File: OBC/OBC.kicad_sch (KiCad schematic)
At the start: 9 parts, among them J2 IDC1 (PMS-Raspi), J3 IDC2 (Raspi-TRU), J5 Conn_01x04, J6 Modo de operación, U1 MPU9250, U2 BMP280, U3 RASPBERRY_PI_ZERO_2_W

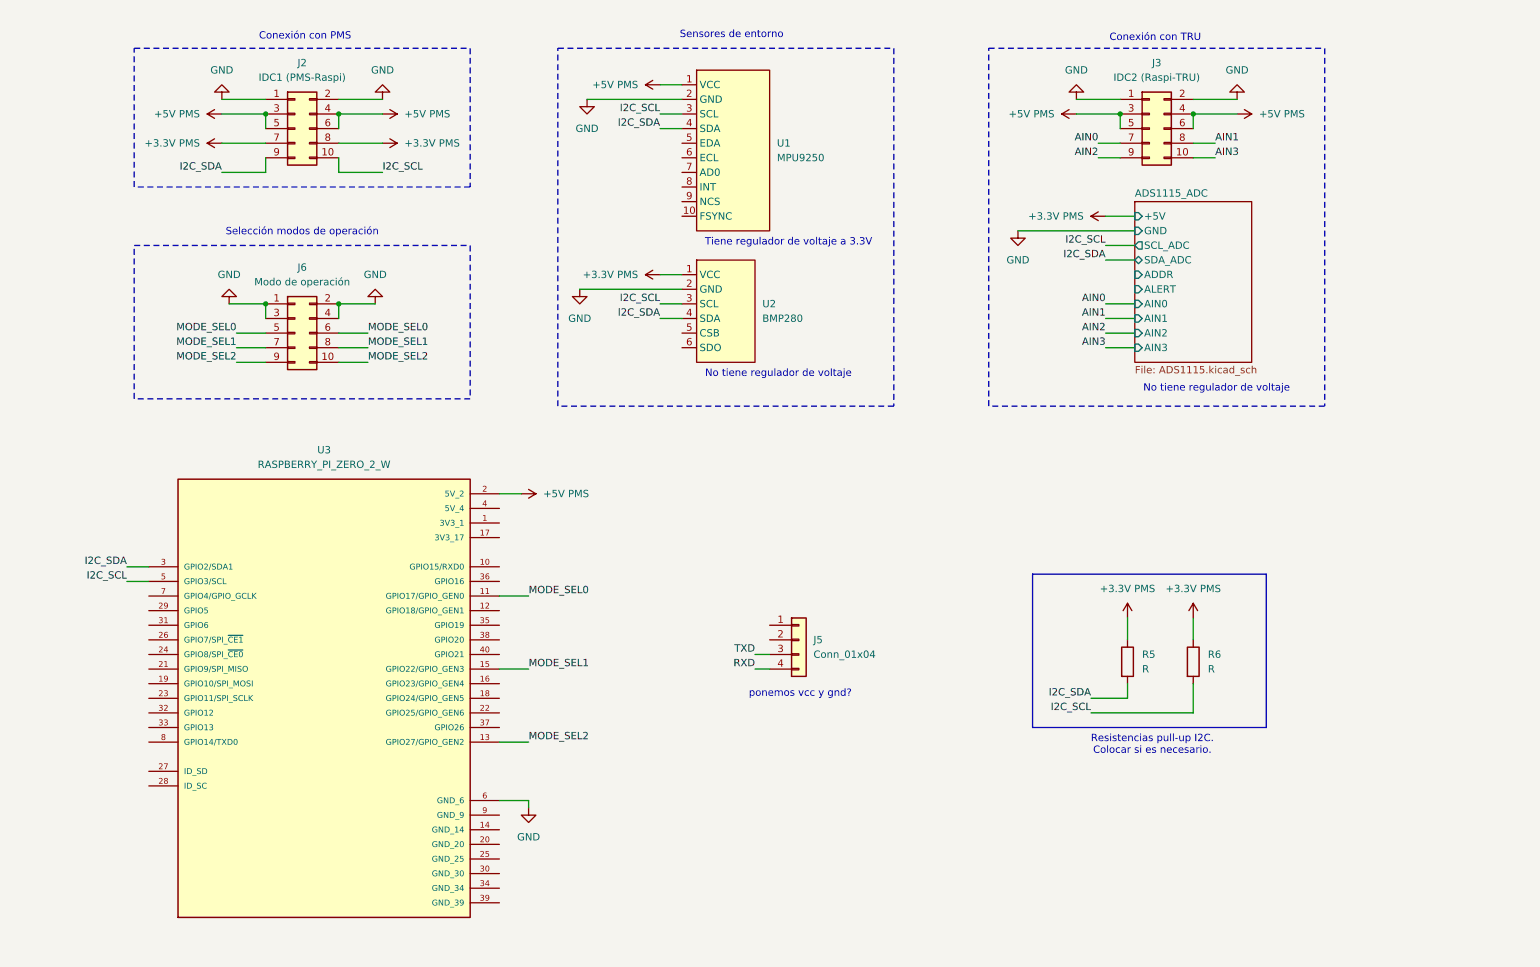
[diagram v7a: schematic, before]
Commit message: Coloca pinout para UART
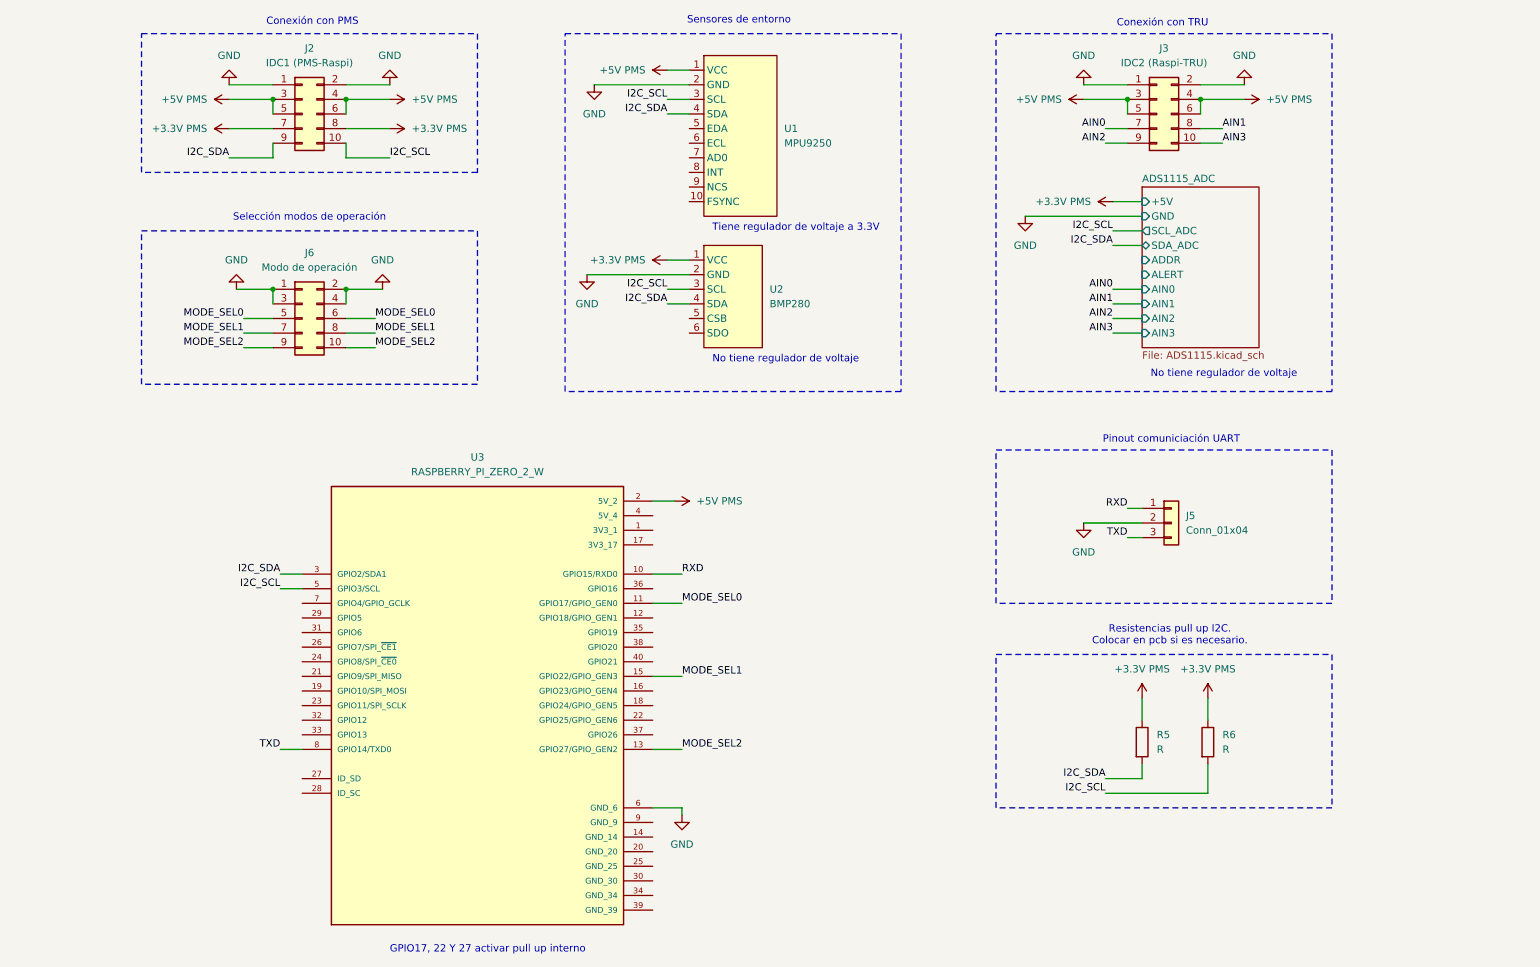
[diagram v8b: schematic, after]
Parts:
- J5: symbol Connector_Generic:Conn_01x04 -> Connector_Generic:Conn_01x03
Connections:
- net GND: now also J5.2 (Pin_2)
- net RXD: now also J5.1 (Pin_1), U3.10 (GPIO15/RXD0); no longer J5.4 (Pin_4)
- net TXD: now also U3.8 (GPIO14/TXD0)
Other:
- note added: "GPIO17, 22 Y 27 activar pull up interno"
- note added: "Pinout comuniciación UART"
- note added: "Resistencias pull up I2C. Colocar en pcb si es necesario."
- note removed: "Resistencias pull-up I2C. Colocar si es necesario."
- note removed: "ponemos vcc y gnd?"
- moved on the sheet: J2, J3, J6, R5, R6, U1, U2, U3
